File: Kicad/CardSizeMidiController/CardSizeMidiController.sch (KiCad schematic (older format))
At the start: 41 parts, among them J1 USB_B, J2 Conn_02x03_Odd_Even, J3 MIDI_OUT, J4 AudioJack3, J5 Screw_Terminal_01x01, J6 Screw_Terminal_01x01, J7 Screw_Terminal_01x01, J8 Screw_Terminal_01x01, SW0 SW_Push, SW1 SW_Push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

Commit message: pcb layout changes
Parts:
- J3: value MIDI_OUT -> MIDI OUT
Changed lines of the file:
@@
 P 7550 1100
 F 0 "J3" H 7550 733 50  0000 C CNN
-F 1 "MIDI_OUT" H 7550 824 50  0000 C CNN
+F 1 "MIDI OUT" H 7550 824 50  0000 C CNN
 F 2 "SensaiLib:din-5" H 7550 1100 50  0001 C CNN
 F 3 "http://www.mouser.com/ds/2/18/40_c091_abd_e-75918.pdf" H 7550 1100 50  0001 C CNN

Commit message: simplified midi code, addeed dual functions, added led brightness adjust, added randomness option
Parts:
- J4: footprint SensaiLib:Jack stereo tayda -> SensaiLib:Jack stereo tayda no extra holes
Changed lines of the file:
@@
 F 0 "J4" H 8370 1783 50  0000 R CNN
 F 1 "AudioJack3" H 8370 1874 50  0000 R CNN
-F 2 "SensaiLib:Jack stereo tayda" H 8650 1850 50  0001 C CNN
+F 2 "SensaiLib:Jack stereo tayda no extra holes" H 8650 1850 50  0001 C CNN
 F 3 "~" H 8650 1850 50  0001 C CNN
 	1    8650 1850

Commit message: new silkscreen design, created logo and labels, minor layout changes
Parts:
- added LOGO1: Logo_Open_Hardware_Small, Card sized midi controller Silckscreen:card sized midi controller logo, symbol Graphic:Logo_Open_Hardware_Small
- added LOGO10: Logo_Open_Hardware_Small, Card sized midi controller Silckscreen:3, symbol Graphic:Logo_Open_Hardware_Small
- added LOGO11: Logo_Open_Hardware_Small, Card sized midi controller Silckscreen:4, symbol Graphic:Logo_Open_Hardware_Small
- added LOGO12: Logo_Open_Hardware_Small, Card sized midi controller Silckscreen:5, symbol Graphic:Logo_Open_Hardware_Small
- added LOGO13: Logo_Open_Hardware_Small, Card sized midi controller Silckscreen:6, symbol Graphic:Logo_Open_Hardware_Small
- added LOGO14, LOGO8: Logo_Open_Hardware_Small, Card sized midi controller Silckscreen:1, symbol Graphic:Logo_Open_Hardware_Small
- added LOGO15: Logo_Open_Hardware_Small, Card sized midi controller Silckscreen:level, symbol Graphic:Logo_Open_Hardware_Small
- added LOGO16: Logo_Open_Hardware_Small, Card sized midi controller Silckscreen:pan, symbol Graphic:Logo_Open_Hardware_Small
- added LOGO17: Logo_Open_Hardware_Small, Card sized midi controller Silckscreen:mod, symbol Graphic:Logo_Open_Hardware_Small
- added LOGO18: Logo_Open_Hardware_Small, Card sized midi controller Silckscreen:cc1, symbol Graphic:Logo_Open_Hardware_Small
- added LOGO19: Logo_Open_Hardware_Small, Card sized midi controller Silckscreen:cc2, symbol Graphic:Logo_Open_Hardware_Small
- added LOGO2: Logo_Open_Hardware_Small, Card sized midi controller Silckscreen:ICSP, symbol Graphic:Logo_Open_Hardware_Small
- added LOGO20: Logo_Open_Hardware_Small, Card sized midi controller Silckscreen:cc3, symbol Graphic:Logo_Open_Hardware_Small
- added LOGO3: Logo_Open_Hardware_Small, Card sized midi controller Silckscreen:midi out, symbol Graphic:Logo_Open_Hardware_Small
- added LOGO4: Logo_Open_Hardware_Small, Card sized midi controller Silckscreen:setting, symbol Graphic:Logo_Open_Hardware_Small
- added LOGO5: Logo_Open_Hardware_Small, Card sized midi controller Silckscreen:rnd, symbol Graphic:Logo_Open_Hardware_Small
- added LOGO6: Logo_Open_Hardware_Small, Card sized midi controller Silckscreen:log, symbol Graphic:Logo_Open_Hardware_Small
- added LOGO7: Logo_Open_Hardware_Small, Card sized midi controller Silckscreen:led, symbol Graphic:Logo_Open_Hardware_Small
- added LOGO9: Logo_Open_Hardware_Small, Card sized midi controller Silckscreen:2, symbol Graphic:Logo_Open_Hardware_Small
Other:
- note added: "1"
- note added: "2"
- note added: "3"
- note added: "4"
- note added: "5"
- note added: "6"
- note added: "cc1"
- note added: "cc2"
- note added: "cc3"
- note added: "icsp"
- note added: "led\n"
- note added: "level"
- note added: "log"
- note added: "logo"
- note added: "midi out"
- note added: "mod"
- note added: "pan"
- note added: "rnd"
- note added: "setting"

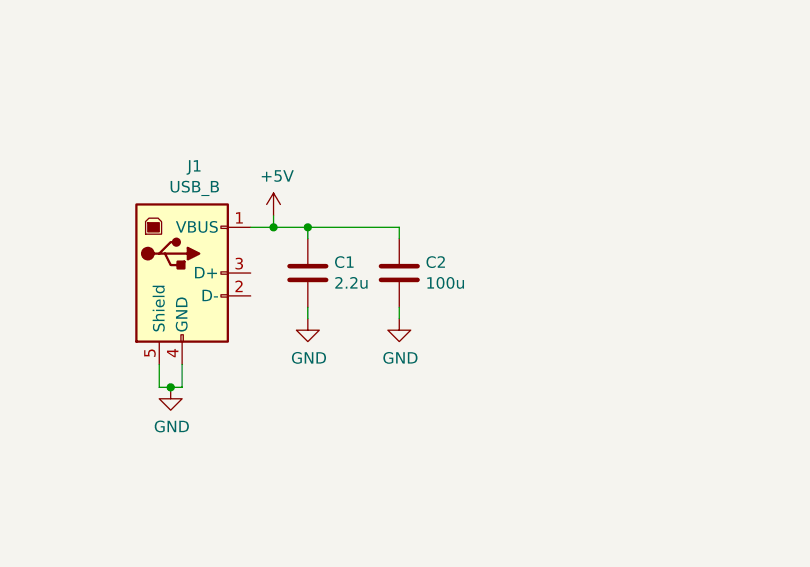
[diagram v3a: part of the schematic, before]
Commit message: changed caps to smd
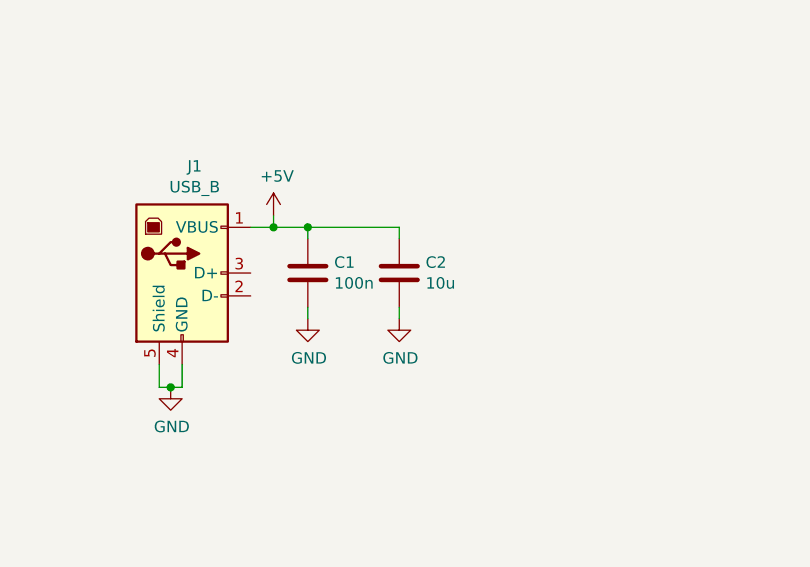
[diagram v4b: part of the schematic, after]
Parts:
- C1: value 2.2u -> 100n; footprint Capacitor_THT:CP_Radial_D5.0mm_P2.50mm -> Capacitor_SMD:C_0805_2012Metric_Pad1.15x1.40mm_HandSolder; LCSC (none) -> C49678
- C2: value 100u -> 10u; footprint Capacitor_THT:CP_Radial_D6.3mm_P2.50mm -> Capacitor_SMD:C_0805_2012Metric_Pad1.15x1.40mm_HandSolder; LCSC (none) -> C15850
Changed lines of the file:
@@
 P 5850 6800
 F 0 "C1" H 5965 6846 50  0000 L CNN
-F 1 "2.2u" H 5965 6755 50  0000 L CNN
-F 2 "Capacitor_THT:CP_Radial_D5.0mm_P2.50mm" H 5888 6650 50  0001 C CNN
+F 1 "100n" H 5965 6755 50  0000 L CNN
+F 2 "Capacitor_SMD:C_0805_2012Metric_Pad1.15x1.40mm_HandSolder" H 5888 6650 50  0001 C CNN
 F 3 "~" H 5850 6800 50  0001 C CNN
+F 4 "C49678" H 5850 6800 50  0001 C CNN "LCSC"
 	1    5850 6800
 	1    0    0    -1
@@
 P 6250 6800
 F 0 "C2" H 6365 6846 50  0000 L CNN
-F 1 "100u" H 6365 6755 50  0000 L CNN
-F 2 "Capacitor_THT:CP_Radial_D6.3mm_P2.50mm" H 6288 6650 50  0001 C CNN
+F 1 "10u" H 6365 6755 50  0000 L CNN
+F 2 "Capacitor_SMD:C_0805_2012Metric_Pad1.15x1.40mm_HandSolder" H 6288 6650 50  0001 C CNN
 F 3 "~" H 6250 6800 50  0001 C CNN
+F 4 "C15850" H 6250 6800 50  0001 C CNN "LCSC"
 	1    6250 6800
 	1    0    0    -1
